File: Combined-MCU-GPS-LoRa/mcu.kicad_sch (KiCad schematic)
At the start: 0 parts

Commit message: Added Readme
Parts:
- added C1, C2: 16p, symbol Device:C
- added U1: ATMEGA168PA-MU, PARTS:VQFN-32_L5.0-W5.0-P0.50-TL-EP, symbol PARTS:ATMEGA168PA-MU
- added Y1: Crystal, symbol Device:Crystal
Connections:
- new net: C2.2, U1.7 ((PCINT6/XTAL1/TOSC1)PB6), Y1.1
- new net: C1.2, U1.8 ((PCINT7/XTAL2/TOSC2)PB7), Y1.2
- new net GND: C1.1, C2.1, U1.21 (GND), U1.3 (GND), U1.33 (EP), U1.5 (GND)
- new net VCC_MCU+: U1.4 (VCC), U1.6 (VCC)

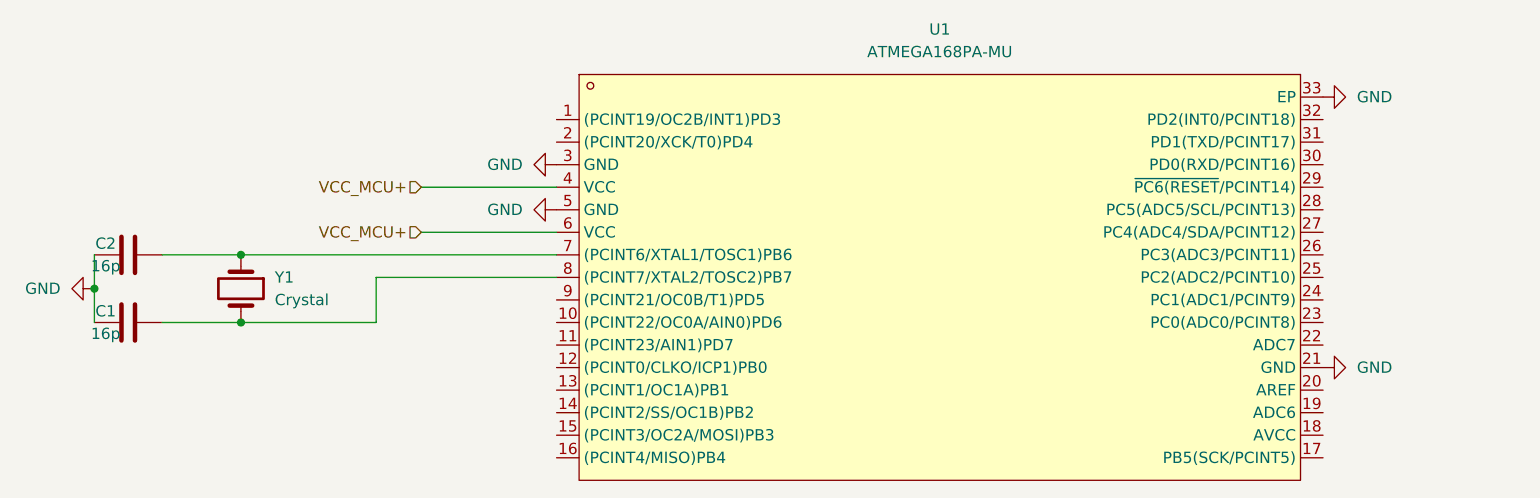
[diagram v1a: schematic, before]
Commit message: I think I have the schematic done.
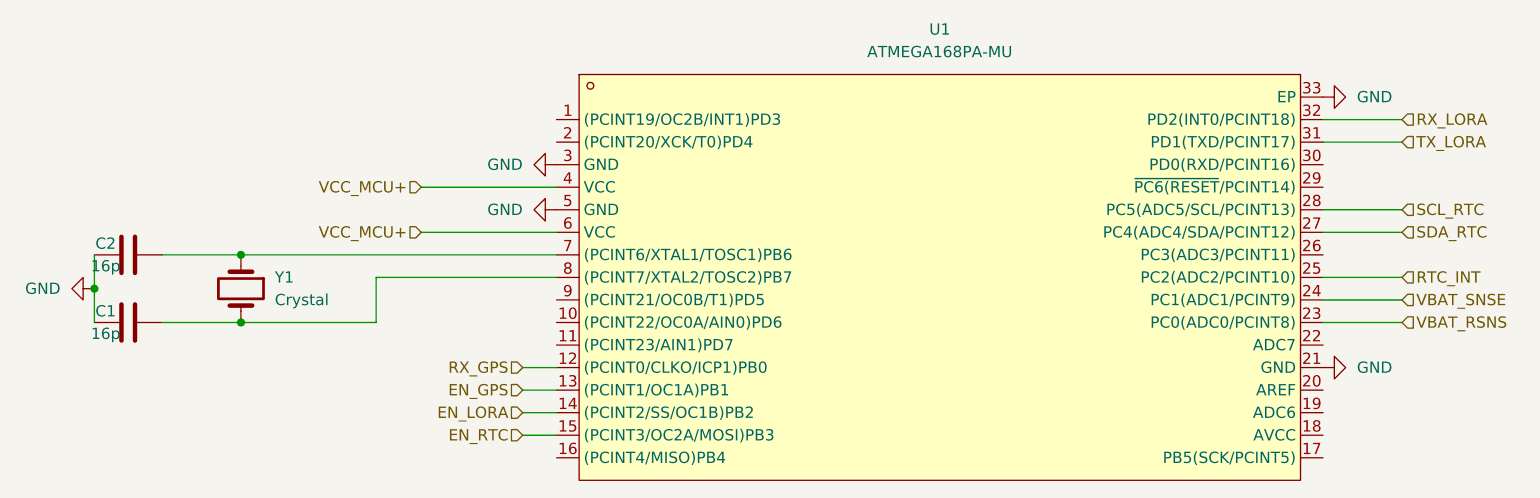
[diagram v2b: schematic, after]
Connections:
- net RX_GPS: now reaches U1.12 ((PCINT0/CLKO/ICP1)PB0)
- net EN_GPS: now reaches U1.13 ((PCINT1/OC1A)PB1)
- net EN_LORA: now reaches U1.14 ((PCINT2/SS/OC1B)PB2)
- net EN_RTC: now reaches U1.15 ((PCINT3/OC2A/MOSI)PB3)
- net VBAT_RSNS: now reaches U1.23 (PC0(ADC0/PCINT8))
- net VBAT_SNSE: now reaches U1.24 (PC1(ADC1/PCINT9))
- net RTC_INT: now reaches U1.25 (PC2(ADC2/PCINT10))
- net SDA_RTC: now reaches U1.27 (PC4(ADC4/SDA/PCINT12))
- net SCL_RTC: now reaches U1.28 (PC5(ADC5/SCL/PCINT13))
- net TX_LORA: now reaches U1.31 (PD1(TXD/PCINT17))
- net RX_LORA: now reaches U1.32 (PD2(INT0/PCINT18))
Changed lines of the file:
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@@
   (junction (at 59.69 83.82) (diameter 0) (color 0 0 0 0)
+  )
+  (wire (pts (xy 207.01 82.55) (xy 198.12 82.55))
+    (stroke (width 0) (type default))
+  )
+  (wire (pts (xy 107.95 97.79) (xy 111.76 97.79))
+    (stroke (width 0) (type default))
   )
   (wire (pts (xy 111.76 82.55) (xy 91.44 82.55))
@@
     (stroke (width 0) (type default))
   )
+  (wire (pts (xy 107.95 95.25) (xy 111.76 95.25))
+    (stroke (width 0) (type default))
+  )
   (wire (pts (xy 91.44 87.63) (xy 76.2 87.63))
     (stroke (width 0) (type default))
   )
+  (wire (pts (xy 207.01 64.77) (xy 198.12 64.77))
+    (stroke (width 0) (type default))
+  )
+  (wire (pts (xy 207.01 85.09) (xy 198.12 85.09))
+    (stroke (width 0) (type default))
+  )
+  (wire (pts (xy 207.01 67.31) (xy 198.12 67.31))
+    (stroke (width 0) (type default))
+  )
   (wire (pts (xy 59.69 80.01) (xy 59.69 83.82))
+    (stroke (width 0) (type default))
+  )
+  (wire (pts (xy 207.01 77.47) (xy 198.12 77.47))
     (stroke (width 0) (type default))
   )
@@
     (stroke (width 0) (type default))
   )
+  (wire (pts (xy 207.01 87.63) (xy 198.12 87.63))
+    (stroke (width 0) (type default))
+  )
+  (wire (pts (xy 107.95 92.71) (xy 111.76 92.71))
+    (stroke (width 0) (type default))
+  )
   (wire (pts (xy 67.31 87.63) (xy 76.2 87.63))
     (stroke (width 0) (type default))
+  )
+  (wire (pts (xy 207.01 74.93) (xy 198.12 74.93))
+    (stroke (width 0) (type default))
+  )
+  (wire (pts (xy 107.95 100.33) (xy 111.76 100.33))
+    (stroke (width 0) (type default))
+  )
+  (hierarchical_label "SCL_RTC" (shape input) (at 207.01 74.93 0) (fields_autoplaced)
+    (effects (font (size 1.27 1.27)) (justify left))
+  )
+  (hierarchical_label "EN_LORA" (shape input) (at 107.95 97.79 180) (fields_autoplaced)
+    (effects (font (size 1.27 1.27)) (justify right))
+  )
+  (hierarchical_label "SDA_RTC" (shape input) (at 207.01 77.47 0) (fields_autoplaced)
+    (effects (font (size 1.27 1.27)) (justify left))
+  )
+  (hierarchical_label "VBAT_SNSE" (shape input) (at 207.01 85.09 0) (fields_autoplaced)
+    (effects (font (size 1.27 1.27)) (justify left))
   )
   (hierarchical_label "VCC_MCU+" (shape input) (at 96.52 77.47 180) (fields_autoplaced)
     (effects (font (size 1.27 1.27)) (justify right))
   )
+  (hierarchical_label "EN_RTC" (shape input) (at 107.95 100.33 180) (fields_autoplaced)
+    (effects (font (size 1.27 1.27)) (justify right))
+  )
+  (hierarchical_label "RTC_INT" (shape input) (at 207.01 82.55 0) (fields_autoplaced)
+    (effects (font (size 1.27 1.27)) (justify left))
+  )
   (hierarchical_label "VCC_MCU+" (shape input) (at 96.52 72.39 180) (fields_autoplaced)
     (effects (font (size 1.27 1.27)) (justify right))
   )
+  (hierarchical_label "RX_GPS" (shape input) (at 107.95 92.71 180) (fields_autoplaced)
+    (effects (font (size 1.27 1.27)) (justify right))
+  )
+  (hierarchical_label "VBAT_RSNS" (shape input) (at 207.01 87.63 0) (fields_autoplaced)
+    (effects (font (size 1.27 1.27)) (justify left))
+  )
+  (hierarchical_label "TX_LORA" (shape input) (at 207.01 67.31 0) (fields_autoplaced)
+    (effects (font (size 1.27 1.27)) (justify left))
+  )
+  (hierarchical_label "RX_LORA" (shape input) (at 207.01 64.77 0) (fields_autoplaced)
+    (effects (font (size 1.27 1.27)) (justify left))
+  )
+  (hierarchical_label "EN_GPS" (shape input) (at 107.95 95.25 180) (fields_autoplaced)
+    (effects (font (size 1.27 1.27)) (justify right))
+  )
